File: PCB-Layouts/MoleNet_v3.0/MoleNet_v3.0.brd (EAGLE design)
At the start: 98.7 x 67.3 mm, 58 parts, among them Q3 BS250, Q4 BS170, Q5 BS250, Q6 BS170, Q7 BS250, Q8 BS170, U1 MCP1703DB, U2 ATMEGA1284p, U4 25LC080P, U5 MCP7940M, U7 BATHOLDER, X1 SMA-142-0711-821/826

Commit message: Updated schematic and board file v3.0
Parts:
- removed JP10, JP12: (no value), pinhead:1X12
- removed R13: 4.7K, rcl:0207/10
- added JP7: (no value), pinhead:1X13
- added JP8: (no value), pinhead:1X11
- moved R10 38.9 mm to (47.0, 25.4)
- moved Q8 38.9 mm to (91.4, 54.6)
- moved Q7 37.0 mm to (86.4, 49.5)
- moved Q5 31.8 mm to (83.8, 57.1)
- moved JP3 26.7 mm to (86.4, 19.1)
- moved R12 23.7 mm to (77.5, 52.1)
- moved R11 23.6 mm to (72.4, 47.0)
- moved JP9 20.9 mm to (22.9, 45.7)
- moved Q6 19.1 mm to (80.0, 43.2), turned to 270 degrees
- moved R9 16.5 mm to (34.3, 25.4), turned to 0 degrees
- moved JP5 13.7 mm to (31.8, 43.2)
- moved C14 13.5 mm to (24.1, 68.6), turned to 180 degrees
- moved L1 10.9 mm to (72.4, 39.4), turned to 0 degrees
- moved Q4 10.2 mm to (20.3, 39.4)
- moved C7 10.2 mm to (66.0, 57.1), turned to 180 degrees
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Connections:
- removed net PCINT23: JP12.3, U2.29
- removed net VSEN+: JP6.2
- net +3V3: no longer R13.2
- net ADC1: now also JP7.1; no longer R13.1
- net ADC2: now also JP7.9; no longer JP10.8
- net ADC3: now also JP7.12; no longer JP10.11
- net ADC4: now also JP7.13; no longer JP10.12
- net ADC5: now also JP7.8; no longer JP10.7
- net ADC6: now also JP7.5; no longer JP10.4
- net ADC7: now also JP7.4; no longer JP10.3
- net ADCVCC: now also JP7.11, JP7.3, JP7.7; no longer JP10.10, JP10.2, JP10.6
- net DIGVCC: now also JP8.2, JP8.5, JP8.9; no longer JP12.10, JP12.2, JP12.6
- net GND: now also JP6.2, JP7.10, JP7.2, JP7.6, JP8.1, JP8.4, JP8.8; no longer JP10.1, JP10.5, JP10.9, JP12.1, JP12.5, JP12.9
- net NSS: now also U2.29
- net PCINT18: now also JP8.11; no longer JP12.12
- net PCINT19: now also JP8.10; no longer JP12.11
- net PCINT20: now also JP8.7; no longer JP12.8
- net PCINT21: now also JP8.6; no longer JP12.7
- net PCINT22: now also JP8.3; no longer JP12.4
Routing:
- net +3V3: track 0.00 -> 280.2 mm
- net RESET: track 0.00 -> 170.2 mm, vias 0 -> 2
- net SCK: track 0.00 -> 155.6 mm, vias 0 -> 2
- net D9: track 0.00 -> 154.0 mm, vias 0 -> 1
- net MISO: track 0.00 -> 107.7 mm, vias 0 -> 2
- net ADC4: track 0.00 -> 85.0 mm, vias 0 -> 3
- net PCINT19: track 0.00 -> 83.3 mm
- net PCINT18: track 0.00 -> 81.9 mm, vias 0 -> 2
- net D7: track 0.00 -> 81.3 mm, vias 0 -> 2
- net D10: track 0.00 -> 80.6 mm, vias 0 -> 1
- net MOSI: track 0.00 -> 76.2 mm, vias 0 -> 2
- net GND: track 0.00 -> 75.9 mm
- net ADCVCC: track 0.00 -> 75.5 mm, vias 0 -> 4
- net TXD1: track 0.00 -> 71.0 mm
- net SCL: track 0.00 -> 70.9 mm
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- added copper zone on layer 16, net GND
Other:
- board size 98.7 x 67.3 mm -> 100 x 67.3 mm
- board text added: "MoleNet v3.0 ComNets"

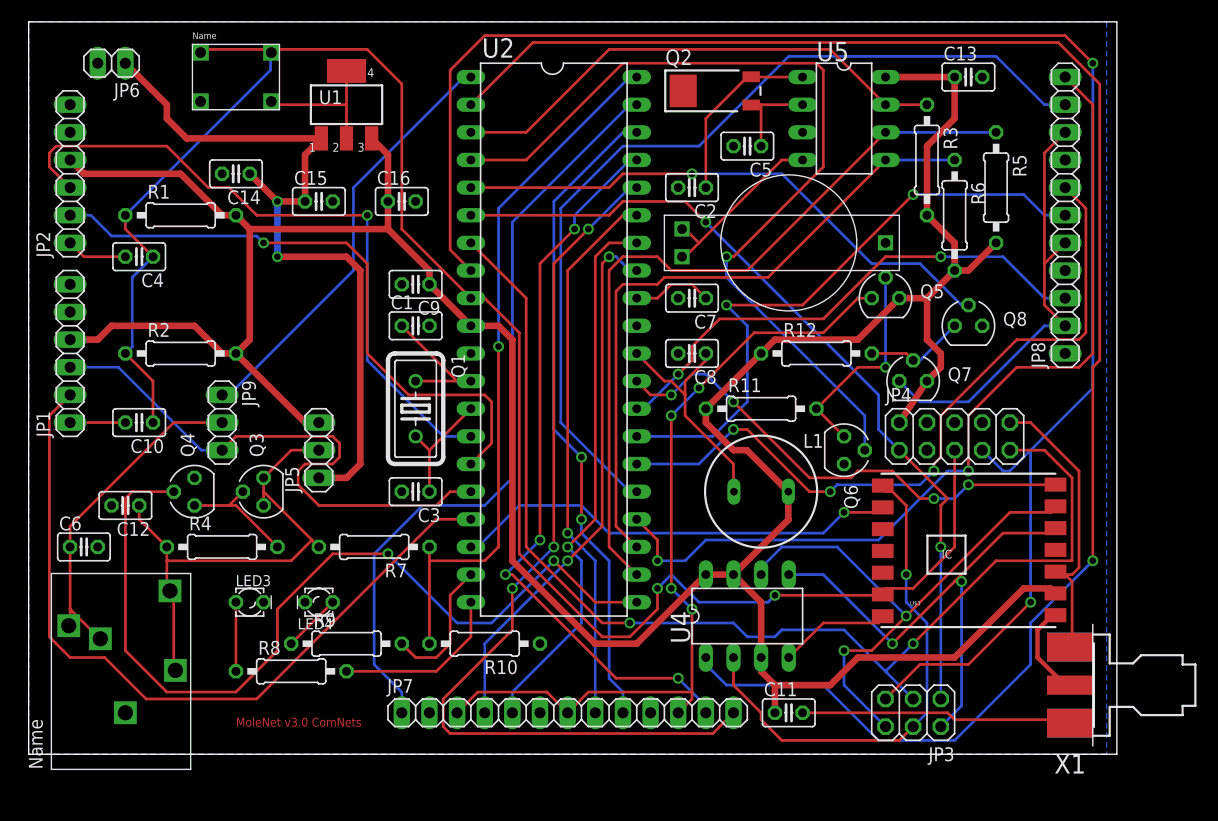
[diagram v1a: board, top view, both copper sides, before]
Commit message: redundant files removed
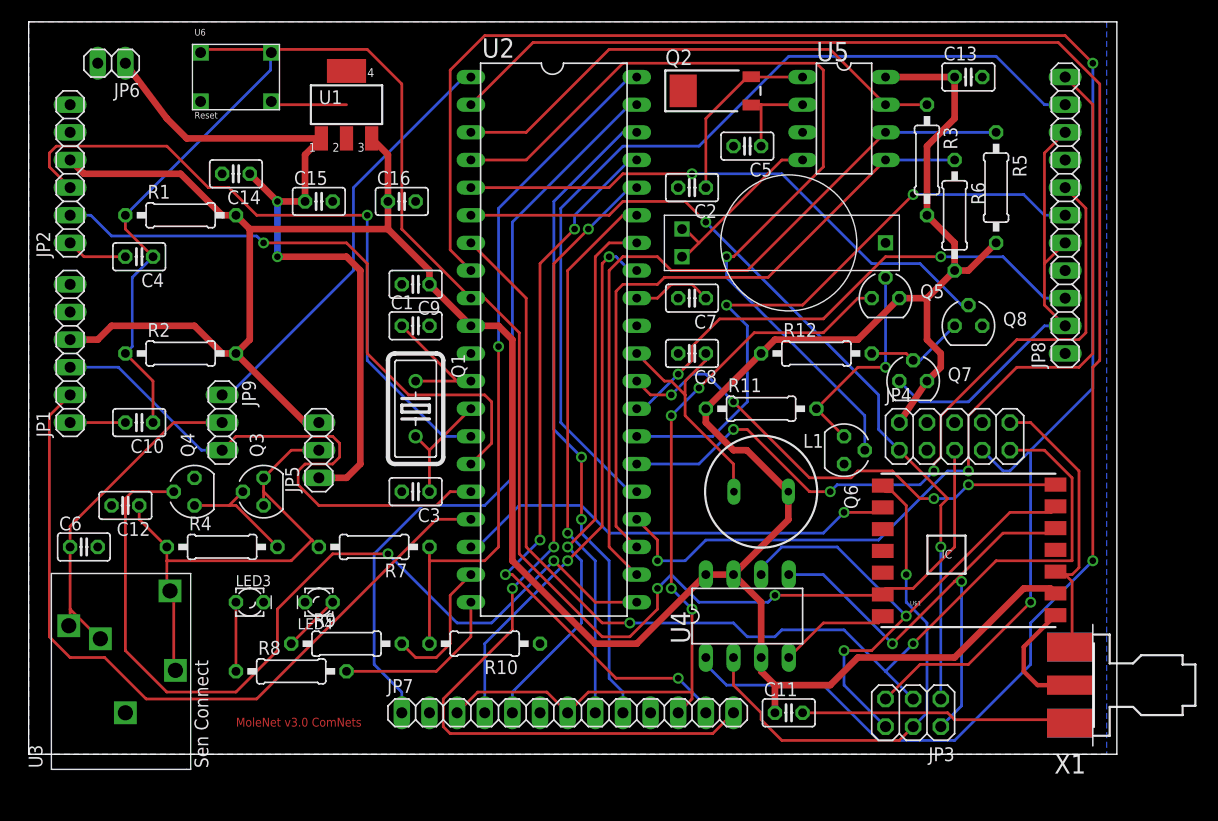
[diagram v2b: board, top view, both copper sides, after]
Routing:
- net GND: track 75.9 -> 69.7 mm
- net N$9: track 8.74 -> 11.1 mm
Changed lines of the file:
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@@
 <contactref element="C5" pad="2"/>
 <contactref element="C13" pad="2"/>
-<contactref element="U1" pad="2"/>
-<contactref element="U1" pad="4"/>
 <contactref element="C14" pad="2"/>
 <contactref element="C15" pad="2"/>
@@
 <wire x1="99.695" y1="31.75" x2="99.44" y2="32.02" width="0.254" layer="1"/>
 <wire x1="100.965" y1="25.4" x2="100.7546" y2="25.0846" width="0.254" layer="1"/>
-<wire x1="34.29" y1="78.029" x2="34.29" y2="74.93" width="0.254" layer="1"/>
-<wire x1="34.29" y1="74.93" x2="34.29" y2="71.8312" width="0.254" layer="1"/>
 <wire x1="78.105" y1="27.305" x2="83.185" y2="27.305" width="0.254" layer="1"/>
 <wire x1="74.93" y1="24.13" x2="78.105" y2="27.305" width="0.254" layer="1"/>
@@
 <wire x1="95.25" y1="45.72" x2="97.155" y2="45.72" width="0.254" layer="1"/>
 <wire x1="100.33" y1="31.75" x2="99.44" y2="32.02" width="0.254" layer="1"/>
+<contactref element="U1" pad="2"/>
+<contactref element="U1" pad="4"/>
+<wire x1="34.29" y1="74.93" x2="34.29" y2="78.029" width="0" layer="19" extent="1-1"/>
+<wire x1="34.29" y1="71.8312" x2="34.29" y2="74.93" width="0" layer="19" extent="1-1"/>
 </signal>
 <signal name="N$1">
@@
 <contactref element="X1" pad="1"/>
 <contactref element="U$1" pad="1"/>
-<wire x1="97.79" y1="26.67" x2="99.06" y2="27.94" width="0.4064" layer="1"/>
-<wire x1="97.79" y1="24.13" x2="97.79" y2="26.67" width="0.4064" layer="1"/>
-<wire x1="100.33" y1="21.59" x2="97.79" y2="24.13" width="0.4064" layer="1"/>
-<wire x1="99.06" y1="27.94" x2="99.44" y2="28.02" width="0.254" layer="1"/>
-<wire x1="100.33" y1="21.59" x2="100.7546" y2="21.59" width="0.254" layer="1"/>
+<wire x1="99.44" y1="28.02" x2="96.52" y2="25.1" width="0.4064" layer="1"/>
+<wire x1="96.52" y1="25.1" x2="96.52" y2="22.86" width="0.4064" layer="1"/>
+<wire x1="96.52" y1="22.86" x2="97.79" y2="21.59" width="0.4064" layer="1"/>
+<wire x1="97.79" y1="21.59" x2="100.7546" y2="21.59" width="0.4064" layer="1"/>
 </signal>
 <signal name="D2">
@@
 <contactref element="C15" pad="1"/>
 <contactref element="JP6" pad="1"/>
-<wire x1="13.97" y1="78.74" x2="17.78" y2="74.93" width="0.6096" layer="1"/>
-<wire x1="17.78" y1="74.93" x2="17.78" y2="73.66" width="0.6096" layer="1"/>
+<wire x1="13.97" y1="78.74" x2="17.78" y2="73.66" width="0.6096" layer="1"/>
 <wire x1="17.78" y1="73.66" x2="19.6088" y2="71.8312" width="0.6096" layer="1"/>
 <wire x1="19.6088" y1="71.8312" x2="31.9786" y2="71.8312" width="0.6096" layer="1"/>
